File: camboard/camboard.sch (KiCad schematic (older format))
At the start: 20 parts

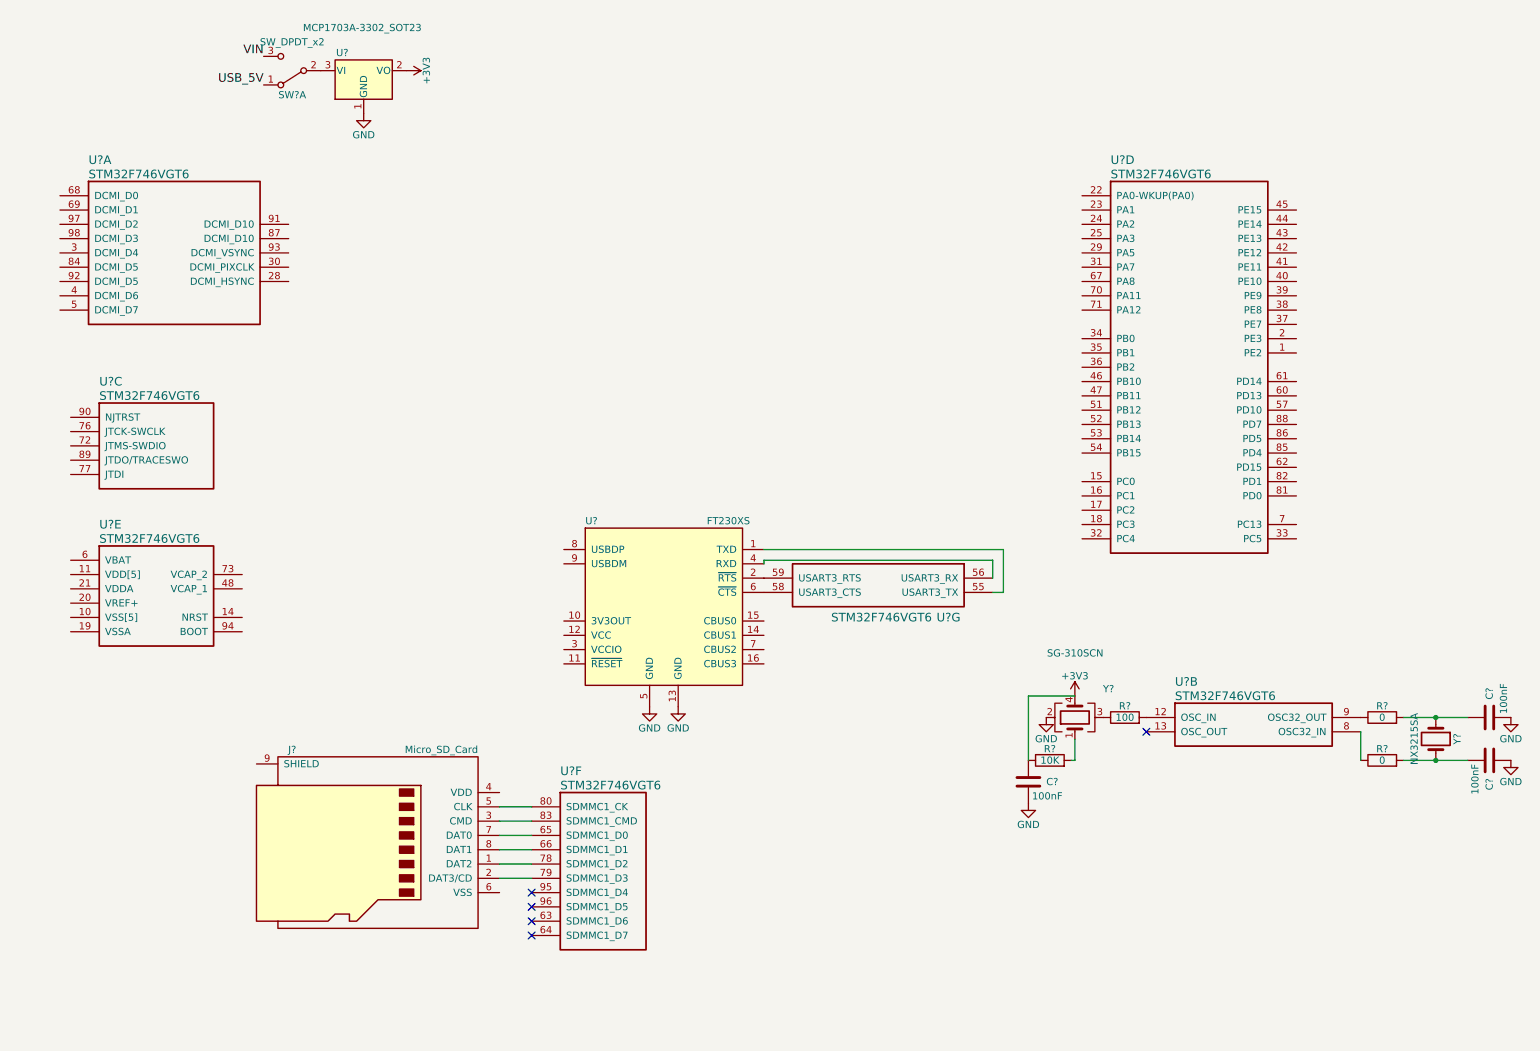
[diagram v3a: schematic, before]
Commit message: added microSD connections, camera very ambiguous
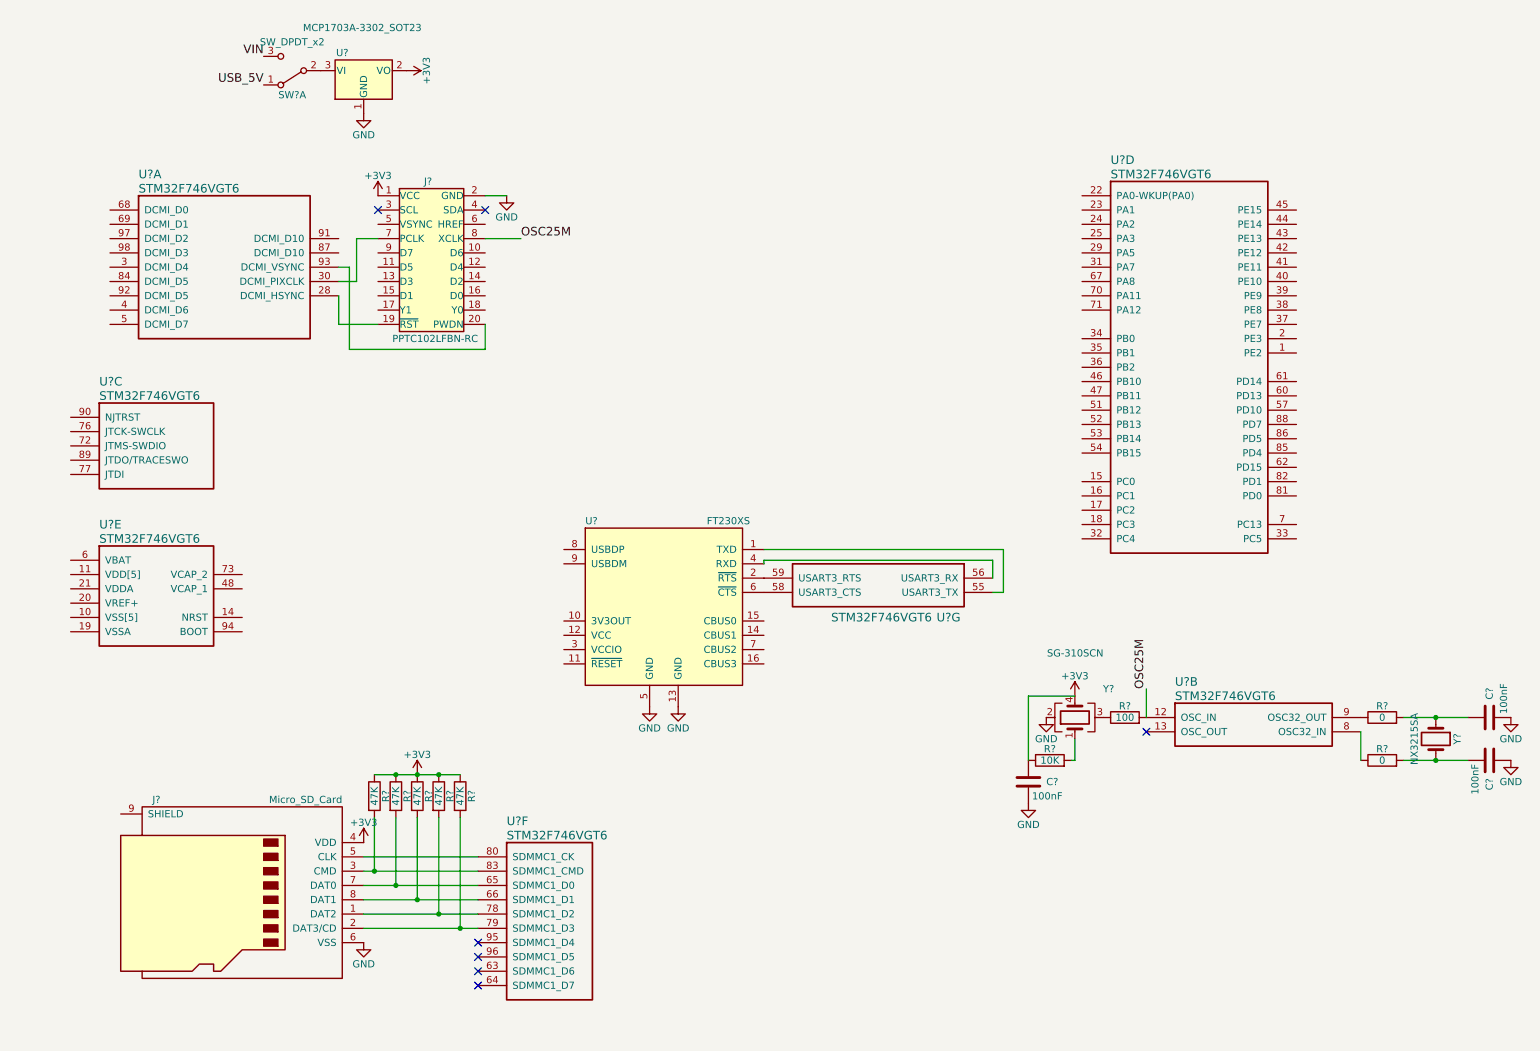
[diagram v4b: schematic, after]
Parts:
- added J?: PPTC102LFBN-RC, Pin_Headers:Pin_Header_Straight_2x10_Pitch2.54mm, symbol PPTC102LFBN-RC
- added R? (x5): 47K, symbol R
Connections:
- net +3V3: now also J?.4 (VDD), J?.1 (VCC), R?.1, R?.1, R?.1, R?.1, R?.1
- net GND: now also J?.6 (VSS), J?.2 (GND)
- net at U?.28 (DCMI_HSYNC): now also J?.19 (~RST)
- net at U?.30 (DCMI_PIXCLK): now also J?.7 (PCLK)
- net at U?.93 (DCMI_VSYNC): now also J?.20 (PWDN)
- net OSC25M: now reaches R?.2, U?.12 (OSC_IN)
- net OSC25M: now also J?.8 (XCLK)
- net at J?.7 (DAT0), U?.65 (SDMMC1_D0): now also R?.2
- net at J?.8 (DAT1), U?.66 (SDMMC1_D1): now also R?.2
- net at J?.1 (DAT2), U?.78 (SDMMC1_D2): now also R?.2
- net at J?.2 (DAT3/CD), U?.79 (SDMMC1_D3): now also R?.2
- net at J?.3 (CMD), U?.83 (SDMMC1_CMD): now also R?.2
- no-connect marks 5 -> 7
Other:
- moved on the sheet: J?, U?A, U?F
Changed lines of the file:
@@
-$Comp
-L STM32F746VGT6 U?
-U 1 1 59CAFAA7
-P 600 1750
-F 0 "U?" H 800 2000 60  0000 L CNN
-F 1 "STM32F746VGT6" H 800 1900 60  0000 L CNN
-F 2 "" H 600 1750 60  0001 C CNN
-F 3 "" H 600 1750 60  0001 C CNN
-	1    600  1750
-	1    0    0    -1
-$EndComp
 $Comp
 L STM32F746VGT6 U?
@@
 Wire Wire Line
 	9700 5500 9700 5700
-NoConn ~ 3900 6925
-NoConn ~ 3900 6825
+NoConn ~ 3525 7275
+NoConn ~ 3525 7175
 $Comp
 L STM32F746VGT6 U?
 U 6 1 59CAFD02
-P 3900 6025
-F 0 "U?" H 4100 6275 60  0000 L CNN
-F 1 "STM32F746VGT6" H 4100 6175 60  0000 L CNN
-F 2 "" H 3900 6025 60  0001 C CNN
-F 3 "" H 3900 6025 60  0001 C CNN
-	6    3900 6025
-	1    0    0    -1
-$EndComp
-NoConn ~ 3900 6725
-NoConn ~ 3900 6625
+P 3525 6375
+F 0 "U?" H 3725 6625 60  0000 L CNN
+F 1 "STM32F746VGT6" H 3725 6525 60  0000 L CNN
+F 2 "" H 3525 6375 60  0001 C CNN
+F 3 "" H 3525 6375 60  0001 C CNN
+	6    3525 6375
+	1    0    0    -1
+$EndComp
+NoConn ~ 3525 7075
+NoConn ~ 3525 6975
 $Comp
 L MCP1703A-3302_SOT23 U?
@@
 L Micro_SD_Card J?
 U 1 1 59CBE1D5
-P 2875 6225
-F 0 "J?" H 2225 6825 50  0000 C CNN
-F 1 "Micro_SD_Card" H 3525 6825 50  0000 R CNN
-F 2 "" V 2575 7175 50  0001 C CNN
-F 3 "" H 2775 6125 50  0001 C CNN
-	1    2875 6225
-	1    0    0    -1
-$EndComp
-Wire Wire Line
-	3675 6025 3900 6025
-Wire Wire Line
-	3900 6125 3675 6125
-Wire Wire Line
-	3675 6225 3900 6225
-Wire Wire Line
-	3675 6325 3900 6325
-Wire Wire Line
-	3900 6425 3675 6425
-Wire Wire Line
-	3675 6525 3900 6525
+P 1925 6575
+F 0 "J?" H 1275 7175 50  0000 C CNN
+F 1 "Micro_SD_Card" H 2575 7175 50  0000 R CNN
+F 2 "" V 1625 7525 50  0001 C CNN
+F 3 "" H 1825 6475 50  0001 C CNN
+	1    1925 6575
+	1    0    0    -1
+$EndComp
+$Comp
+L GND #PWR?
+U 1 1 59CBEA54
+P 2725 6975
+F 0 "#PWR?" H 2725 6725 50  0001 C CNN
+F 1 "GND" H 2725 6825 50  0000 C CNN
+F 2 "" H 2725 6975 50  0001 C CNN
+F 3 "" H 2725 6975 50  0001 C CNN
+	1    2725 6975
+	1    0    0    -1
+$EndComp
+$Comp
+L +3V3 #PWR?
+U 1 1 59CBEA9B
+P 3100 5800
+F 0 "#PWR?" H 3100 5650 50  0001 C CNN
+F 1 "+3V3" H 3100 5940 50  0000 C CNN
+F 2 "" H 3100 5800 50  0001 C CNN
+F 3 "" H 3100 5800 50  0001 C CNN
+	1    3100 5800
+	1    0    0    -1
+$EndComp
+$Comp
+L R R?
+U 1 1 59CBEC1A
+P 2800 5950
+F 0 "R?" V 2880 5950 50  0000 C CNN
+F 1 "47K" V 2800 5950 50  0000 C CNN
+F 2 "" V 2730 5950 50  0001 C CNN
+F 3 "" H 2800 5950 50  0001 C CNN
+	1    2800 5950
+	1    0    0    -1
+$EndComp
+$Comp
+L R R?
+U 1 1 59CBEF3E
+P 2950 5950
+F 0 "R?" V 3030 5950 50  0000 C CNN
+F 1 "47K" V 2950 5950 50  0000 C CNN
+F 2 "" V 2880 5950 50  0001 C CNN
+F 3 "" H 2950 5950 50  0001 C CNN
+	1    2950 5950
+	1    0    0    -1
+$EndComp
+$Comp
+L R R?
+U 1 1 59CBEFC6
+P 3100 5950
+F 0 "R?" V 3180 5950 50  0000 C CNN
+F 1 "47K" V 3100 5950 50  0000 C CNN
+F 2 "" V 3030 5950 50  0001 C CNN
+F 3 "" H 3100 5950 50  0001 C CNN
+	1    3100 5950
+	1    0    0    -1
+$EndComp
+$Comp
+L R R?
+U 1 1 59CBF027
+P 3250 5950
+F 0 "R?" V 3330 5950 50  0000 C CNN
+F 1 "47K" V 3250 5950 50  0000 C CNN
+F 2 "" V 3180 5950 50  0001 C CNN
+F 3 "" H 3250 5950 50  0001 C CNN
+	1    3250 5950
+	1    0    0    -1
+$EndComp
+$Comp
+L R R?
+U 1 1 59CBF089
+P 3400 5950
+F 0 "R?" V 3480 5950 50  0000 C CNN
+F 1 "47K" V 3400 5950 50  0000 C CNN
+F 2 "" V 3330 5950 50  0001 C CNN
+F 3 "" H 3400 5950 50  0001 C CNN
+	1    3400 5950
+	1    0    0    -1
+$EndComp
+$Comp
+L +3V3 #PWR?
+U 1 1 59CBF0F6
+P 2725 6275
+F 0 "#PWR?" H 2725 6125 50  0001 C CNN
+F 1 "+3V3" H 2725 6415 50  0000 C CNN
+F 2 "" H 2725 6275 50  0001 C CNN
+F 3 "" H 2725 6275 50  0001 C CNN
+	1    2725 6275
+	1    0    0    -1
+$EndComp
+Wire Wire Line
+	2725 6475 3525 6475
+Wire Wire Line
+	2800 6475 2800 6100
+Wire Wire Line
+	2725 6575 3525 6575
+Wire Wire Line
+	2950 6575 2950 6100
+Wire Wire Line
+	2725 6675 3525 6675
+Wire Wire Line
+	3100 6675 3100 6100
+Wire Wire Line
+	2725 6775 3525 6775
+Wire Wire Line
+	3250 6775 3250 6100
+Wire Wire Line
+	2725 6875 3525 6875
+Wire Wire Line
+	3400 6875 3400 6100
+Wire Wire Line
+	2725 6375 3525 6375
+Connection ~ 2800 6475
+Connection ~ 2950 6575
+Connection ~ 3100 6675
+Connection ~ 3250 6775
+Connection ~ 3400 6875
+Wire Wire Line
+	2800 5800 3400 5800
+Connection ~ 2950 5800
+Connection ~ 3100 5800
+Connection ~ 3250 5800
+$Comp
+L PPTC102LFBN-RC J?
+U 1 1 59CC1D8B
+P 3025 2150
+F 0 "J?" H 3175 2650 50  0000 C CNN
+F 1 "PPTC102LFBN-RC" H 3225 1550 50  0000 C CNN
+F 2 "Pin_Headers:Pin_Header_Straight_2x10_Pitch2.54mm" H 1675 2000 50  0001 C CNN
+F 3 "" H 3325 2650 50  0001 C CNN
+	1    3025 2150
+	1    0    0    -1
+$EndComp
+Wire Wire Line
+	2550 2350 2675 2350
+Wire Wire Line
+	2675 2350 2675 2050
+Wire Wire Line
+	2675 2050 2825 2050
+Text Label 8200 5200 1    60   ~ 0
+OSC25M
+Wire Wire Line
+	8200 5400 8200 5200
+Text Label 3825 2050 0    60   ~ 0
+OSC25M
+$Comp
+L STM32F746VGT6 U?
+U 1 1 59CAFAA7
+P 950 1850
+F 0 "U?" H 1150 2100 60  0000 L CNN
+F 1 "STM32F746VGT6" H 1150 2000 60  0000 L CNN
+F 2 "" H 950 1850 60  0001 C CNN
+F 3 "" H 950 1850 60  0001 C CNN
+	1    950  1850
+	1    0    0    -1
+$EndComp
+Wire Wire Line
+	2825 2650 2550 2650
+Wire Wire Line
+	2550 2650 2550 2450
+Wire Wire Line
+	2550 2250 2625 2250
+Wire Wire Line
+	2625 2250 2625 2825
+Wire Wire Line
+	2625 2825 3575 2825
+Wire Wire Line
+	3575 2825 3575 2650
+NoConn ~ 2825 1850
+NoConn ~ 3575 1850
+$Comp
+L +3V3 #PWR?
+U 1 1 59CC45D1
+P 2825 1750
+F 0 "#PWR?" H 2825 1600 50  0001 C CNN
+F 1 "+3V3" H 2825 1890 50  0000 C CNN
+F 2 "" H 2825 1750 50  0001 C CNN
+F 3 "" H 2825 1750 50  0001 C CNN
+	1    2825 1750
+	1    0    0    -1
+$EndComp
+$Comp
+L GND #PWR?
+U 1 1 59CC4735
+P 3725 1750
+F 0 "#PWR?" H 3725 1500 50  0001 C CNN
+F 1 "GND" H 3725 1600 50  0000 C CNN
+F 2 "" H 3725 1750 50  0001 C CNN
+F 3 "" H 3725 1750 50  0001 C CNN
+	1    3725 1750
+	1    0    0    -1
+$EndComp
+Wire Wire Line
+	3575 1750 3725 1750
+Wire Wire Line
+	3825 2050 3575 2050
 $EndSCHEMATC

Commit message: added JTAG Connection
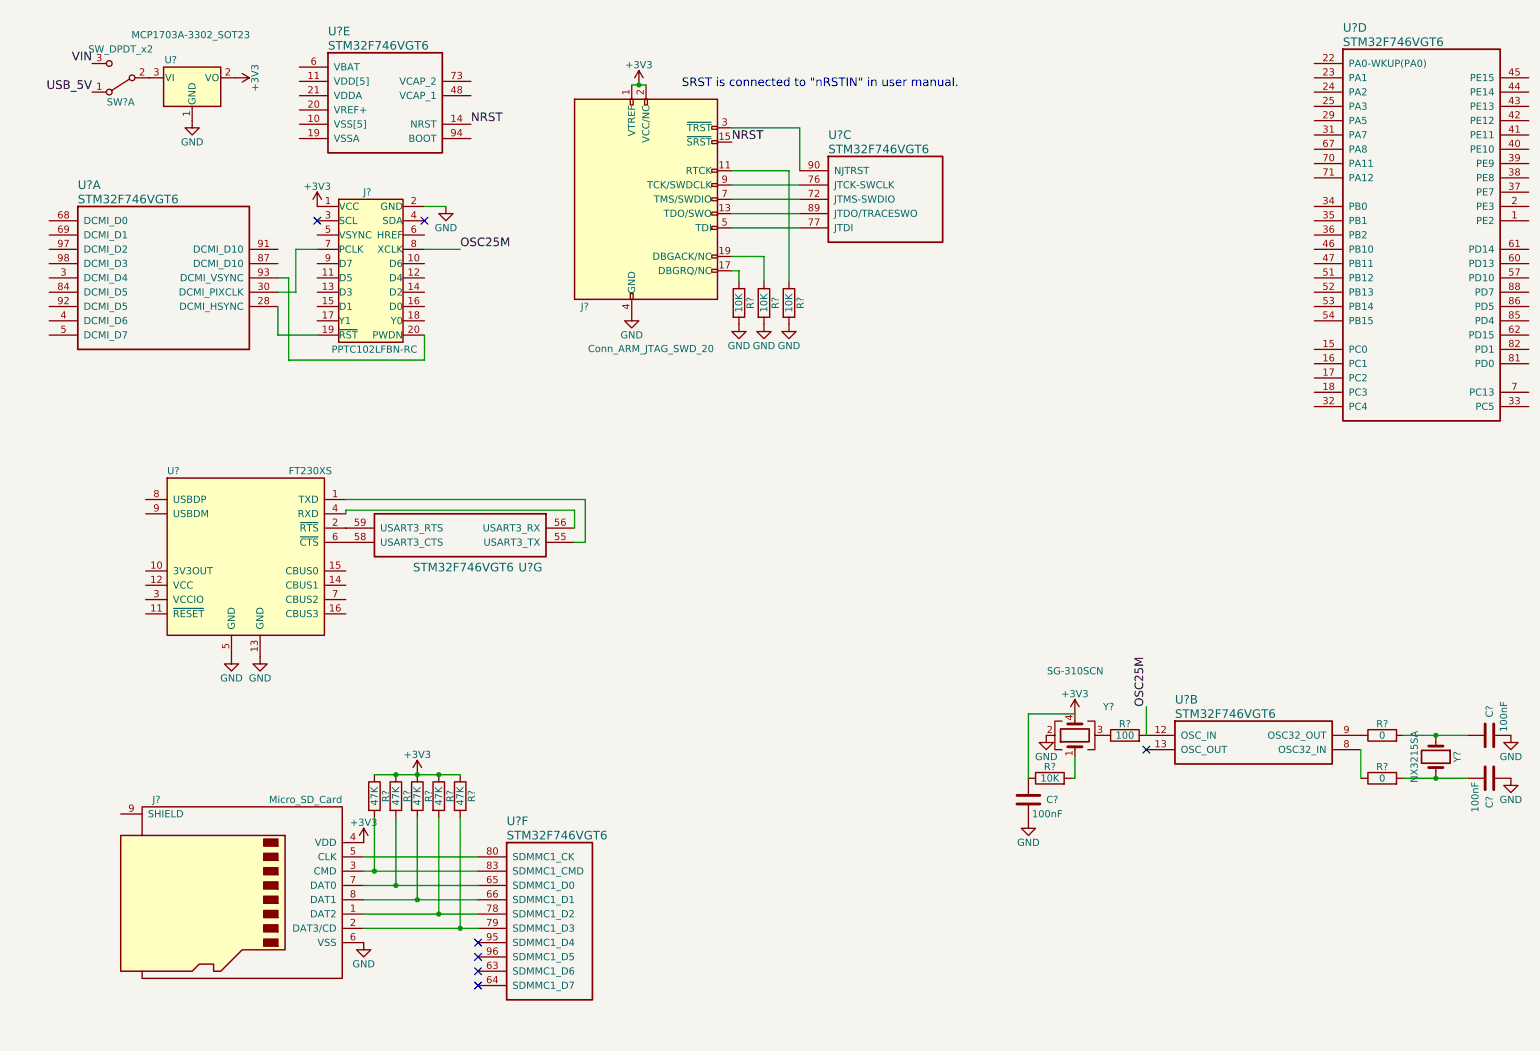
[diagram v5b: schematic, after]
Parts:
- added J?: Conn_ARM_JTAG_SWD_20, symbol Conn_ARM_JTAG_SWD_20
- added R? (x3): 10K, symbol R
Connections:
- net +3V3: now also J?.1 (VTREF), J?.2 (VCC/NC)
- net GND: now also J?.10 (GND), J?.12 (GND), J?.14 (GND), J?.16 (GND), J?.18 (GND), J?.20 (GND), J?.4 (GND), J?.6 (GND), J?.8 (GND), R?.2, R?.2, R?.2
- net at U?.72 (JTMS-SWDIO): now also J?.7 (TMS/SWDIO)
- net at U?.76 (JTCK-SWCLK): now also J?.9 (TCK/SWDCLK)
- net at U?.77 (JTDI): now also J?.5 (TDI)
- net at U?.89 (JTDO/TRACESWO): now also J?.13 (TDO/SWO)
- net at U?.90 (NJTRST): now also J?.3 (~TRST~)
- net NRST: now reaches U?.14 (NRST)
- net NRST: now also J?.15 (~SRST~)
- new net: J?.11 (RTCK), R?.1
- new net: J?.17 (DBGRQ/NC), R?.1
- new net: J?.19 (DBGACK/NC), R?.1
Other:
- note added: "SRST is connected to "nRSTIN" in user manual."
- moved on the sheet: C?, J?, R?, SW?A, U?, U?A, U?B, U?C, U?D, U?E, U?G, Y?
